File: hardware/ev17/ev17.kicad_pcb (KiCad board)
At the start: 4 copper layers, 125 x 80 mm, 185 parts, among them CN1 Conn_05x02_Female, CN2 PJ-242, J1 USB_C_Receptacle, J10 Conn_02x05_Counter_Clockwise, J11 Conn_02x05_Counter_Clockwise, J17 Conn_01x01, J18 Conn_01x01, J19 Conn_01x01, J2 Conn_01x02_Socket, J3 AudioJack4, J4 Conn_02x03_Odd_Even, J5 Conn_02x03_Odd_Even, J6 Conn_02x05_Counter_Clockwise, J7 Conn_02x05_Counter_Clockwise, J8 Conn_02x05_Counter_Clockwise, J9 Conn_02x05_Counter_Clockwise, Q1 2N7002, Q2 2N7002, Q3 2N7002, SW1 SW_SPDT, SW2 SW_Push, SW3 SW_Push, SW4 SW_Push, SW5 SW_Push, SW6 SW_Push, SW7 SW_Push, U1 BQ21040DBV, U10 STM32F405RGTx, U12 XC6227C301MR-G, U2 USBLC6-2P6, U3 STM32F072CBTx, U4 CH340C, U5 TPS63060, U6 WM8960CGEFL/RV, U7 ESP32-S3-WROOM-1, U8 M24C02-RMN6TP, U9 TPS2116DRL, Y1 Crystal_GND24

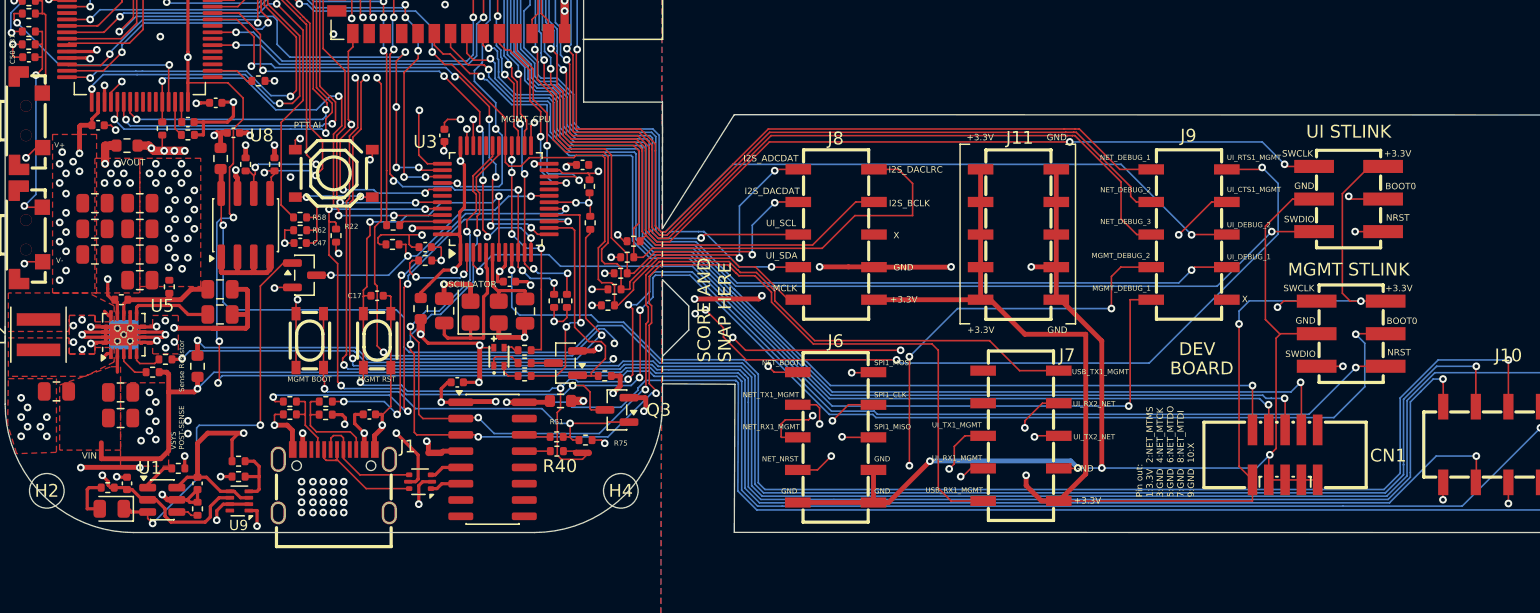
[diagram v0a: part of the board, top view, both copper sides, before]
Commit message: Moved the position of the battery charger and added a heat sink area (refs #147, #127)
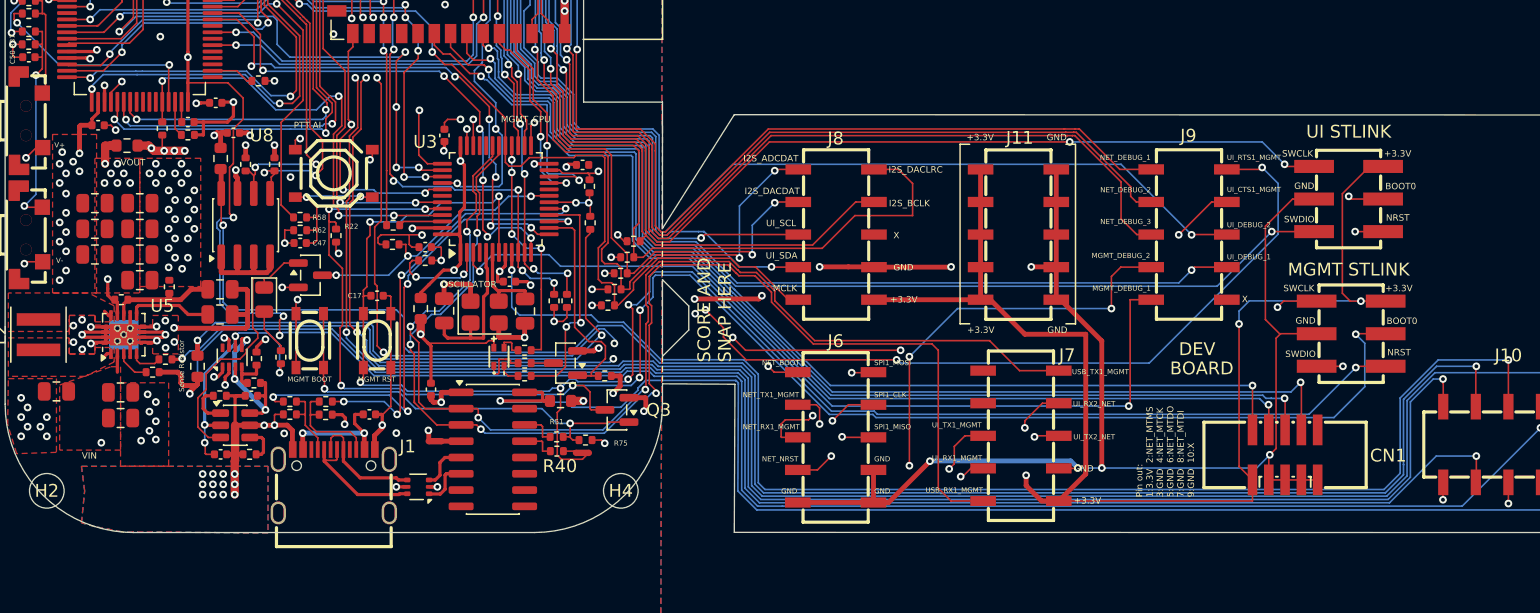
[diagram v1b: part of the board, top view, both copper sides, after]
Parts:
- moved D1 20.2 mm to (70.2, 91.8), turned to -90 degrees
- moved R11 16.9 mm to (71.5, 96.3), turned to 90 degrees
- moved U9 11.2 mm to (67.7, 96.3), turned to 90 degrees
- moved R47 9.31 mm to (69.6, 96.4), turned to -90 degrees
- moved U1 8.13 mm to (67.9, 101.6)
- moved C4 8.02 mm to (69.2, 99.3), turned to 180 degrees
- moved C12 7.64 mm to (66.8, 103.9), turned to 0 degrees
- moved R6 6.52 mm to (66.7, 99.3)
- moved R53 6.22 mm to (69.4, 98.3), turned to 0 degrees
- moved R1 5.87 mm to (69.1, 103.9), turned to 180 degrees
- moved C13 2.12 mm to (83.2, 98.8), turned to -90 degrees
- moved NT2 0.91 mm to (83.5, 102.9)
- moved U4 0.78 mm to (88.0, 103.5)
- moved Q2 0.46 mm to (73.8, 89.9)
- moved U2 0.43 mm to (82.2, 106.4)
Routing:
- net GND: track 386.4 -> 363.8 mm, vias 168 -> 155
- net Net-(J2-Pin_2): track 78.5 -> 91.5 mm, vias 2 -> 5
- net Net-(D1-K): track 31.1 -> 21.9 mm, vias 2 -> 0
- net /BB_Vin_Sense: track 131.2 -> 137.0 mm, vias 2 -> 3
- net +3.3V: track 267.4 -> 262.3 mm, vias 69 -> 65
- net Net-(SW1-C): track 76.2 -> 72.5 mm, vias 1 -> 2
- net VBUS: track 37.8 -> 34.9 mm, vias 4 -> 8
- net /UI_Sense: track 197.2 -> 194.3 mm
- net /BB_Vout_Sense: track 132.2 -> 134.8 mm
- net VSYS: track 184.8 -> 187.1 mm
- net /CH340C_Sense: track 107.7 -> 109.7 mm
- net /D_N: track 9.17 -> 11.0 mm
- net /WM8960_Sense: track 192.7 -> 191.1 mm
- net Net-(U9-PR1): track 5.01 -> 3.45 mm
- net /USB_RX1_MGMT: track 96.6 -> 95.1 mm
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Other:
- board text removed: "VSYS POST-SENSE"

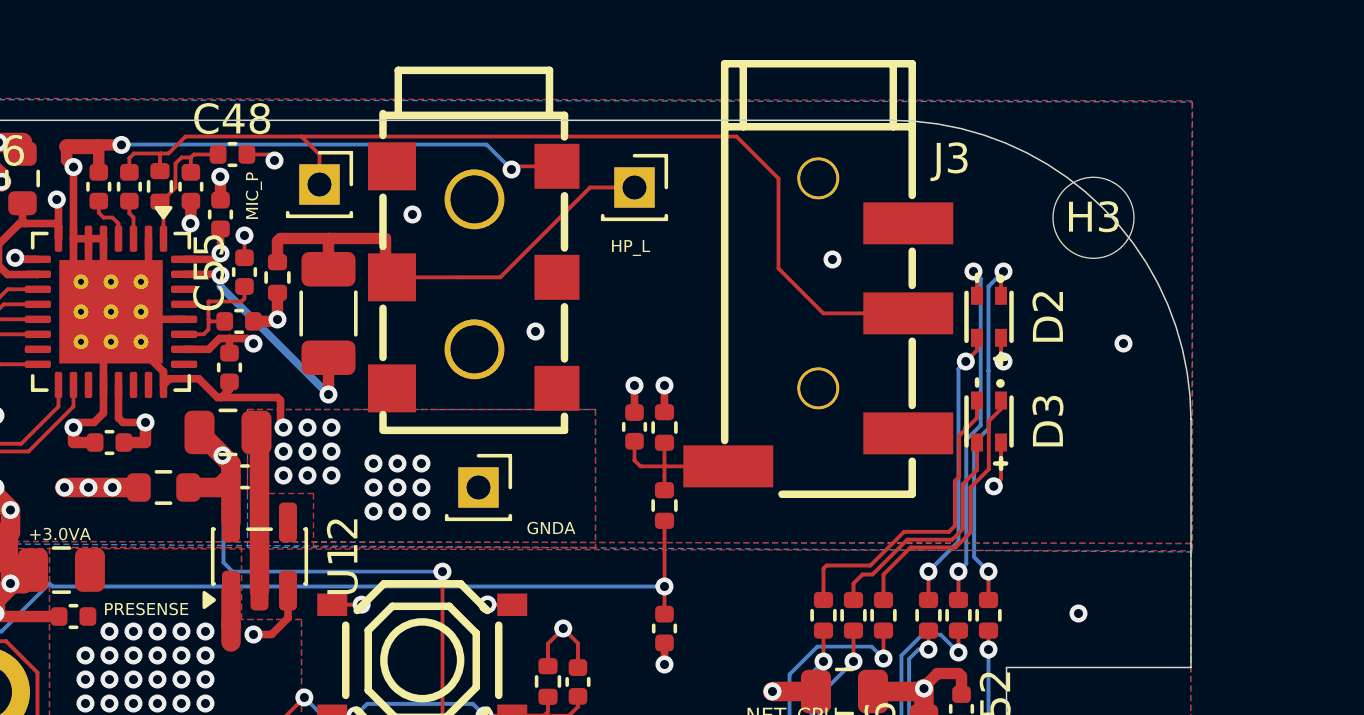
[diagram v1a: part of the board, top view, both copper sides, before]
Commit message: Added labels for the jacks (refs #410)
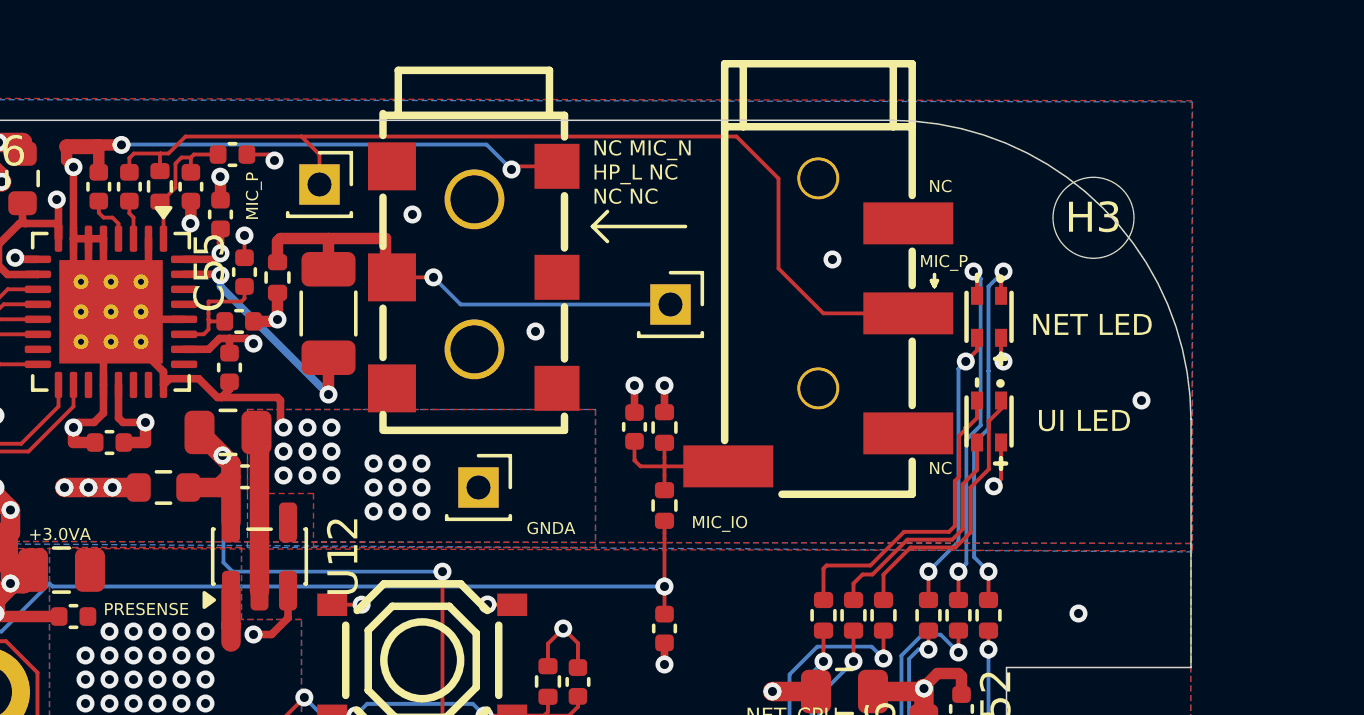
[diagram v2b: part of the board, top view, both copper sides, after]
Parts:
- moved J17 4.08 mm to (83.9, 36.1)
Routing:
- net /HP_L: track 15.9 -> 16.4 mm, vias 0 -> 1
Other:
- board text added: "MIC_IO"
- board text added: "NC"
- board text added: "NC MIC_N HP_L NC NC NC"
- board text added: "NET LED"
- board text added: "UI LED"
- board text removed: "HP_L"
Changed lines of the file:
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@@
 			(at 0 -1.16 0)
 			(layer "F.SilkS")
+			(hide yes)
 			(effects
 				(font
@@
 			(at 4.45 -6.195 0)
 			(layer "F.SilkS")
+			(hide yes)
 			(effects
 				(font
@@
 	(footprint "Connector_PinSocket_2.00mm:PinSocket_1x01_P2.00mm_Vertical"
 		(layer "F.Cu")
-		(at 82.7 32.24)
+		(at 83.9 36.14)
 		(descr "Through hole straight socket strip, 1x01, 2.00mm pitch, single row (from Kicad 4.0.7), script generated")
 		(tags "Through hole socket strip THT 1x01 2.00mm single row")
@@
 			(at 0 -2 90)
 			(layer "F.SilkS")
+			(hide yes)
 			(effects
 				(font
@@
 			(at 0 -2 90)
 			(layer "F.SilkS")
+			(hide yes)
 			(effects
 				(font
@@
 	)
 	(gr_line
+		(start 81.3 33.54)
+		(end 81.8 34.04)
+		(stroke
+			(width 0.12)
+			(type default)
+		)
+		(layer "F.SilkS")
+	)
+	(gr_line
 		(start 101.25 86.54)
 		(end 101.25 90.34)
@@
 	)
 	(gr_line
+		(start 92.7 35.54)
+		(end 92.6 35.34)
+		(stroke
+			(width 0.12)
+			(type default)
+		)
+		(layer "F.SilkS")
+	)
+	(gr_line
 		(start 125.2 79.73)
 		(end 124.45 79.73)
@@
 	)
 	(gr_line
+		(start 81.3 33.54)
+		(end 81.8 33.04)
+		(stroke
+			(width 0.12)
+			(type default)
+		)
+		(layer "F.SilkS")
+	)
+	(gr_line
 		(start 69.4 57.39)
 		(end 69.4 55.29)
@@
 	)
 	(gr_line
+		(start 92.7 35.14)
+		(end 92.7 35.54)
+		(stroke
+			(width 0.12)
+			(type default)
+		)
+		(layer "F.SilkS")
+	)
+	(gr_line
 		(start 70.2 57.04)
 		(end 70.2 55.94)
@@
 	)
 	(gr_line
+		(start 92.6 35.34)
+		(end 92.7 35.54)
+		(stroke
+			(width 0.12)
+			(type default)
+		)
+		(layer "F.SilkS")
+	)
+	(gr_line
+		(start 92.7 35.54)
+		(end 92.8 35.34)
+		(stroke
+			(width 0.12)
+			(type default)
+		)
+		(layer "F.SilkS")
+	)
+	(gr_line
+		(start 84.4 33.54)
+		(end 81.3 33.54)
+		(stroke
+			(width 0.12)
+			(type default)
+		)
+		(layer "F.SilkS")
+	)
+	(gr_line
 		(start 71 56.99)
 		(end 71 56.64)
@@
 		)
 	)
+	(gr_text "MIC_IO"
+		(at 84.6 43.64 0)
+		(layer "F.SilkS")
+		(effects
+			(font
+				(size 0.4 0.4)
+				(thickness 0.1)
+			)
+			(justify left bottom)
+		)
+	)
+	(gr_text "UI LED"
+		(at 96.1 40.44 0)
+		(layer "F.SilkS")
+		(effects
+			(font
+				(size 0.7 0.7)
+				(thickness 0.1)
+			)
+			(justify left bottom)
+		)
+	)
 	(gr_text "SWCLK"
 		(at 149.65 91.25 0)
@@
 		)
 	)
+	(gr_text "NET LED"
+		(at 95.9 37.24 0)
+		(layer "F.SilkS")
+		(effects
+			(font
+				(size 0.7 0.7)
+				(thickness 0.1)
+			)
+			(justify left bottom)
+		)
+	)
 	(gr_text "UI_RX1_MGMT"
 		(at 122.25 104.43 0)
@@
 		)
 	)
+	(gr_text "NC"
+		(at 92.5 32.44 0)
+		(layer "F.SilkS")
+		(effects
+			(font
+				(size 0.4 0.4)
+				(thickness 0.1)
+			)
+			(justify left bottom)
+		)
+	)
 	(gr_text "X"
 		(at 119.25 87.125 0)
@@
 		)
 	)
+	(gr_text "NC"
+		(at 92.5 41.84 0)
+		(layer "F.SilkS")
+		(effects
+			(font
+				(size 0.4 0.4)
+				(thickness 0.1)
+			)
+			(justify left bottom)
+		)
+	)
 	(gr_text "PRESENSE"
 		(at 65 46.54 0)
@@
 		)
 	)
-	(gr_text "HP_L"
-		(at 81.9 34.44 0)
+	(gr_text "NC MIC_N\nHP_L NC\nNC NC"
+		(at 81.3 32.84 0)
 		(layer "F.SilkS")
 		(effects
 			(font
-				(size 0.4 0.4)
+				(size 0.5 0.5)
 				(thickness 0.1)
 			)
@@
 		)
 	)
+	(gr_text "MIC_P"
+		(at 92.2 34.94 0)
+		(layer "F.SilkS")
+		(effects
+			(font
+				(size 0.4 0.4)
+				(thickness 0.1)
+			)
+			(justify left bottom)
+		)
+	)
 	(gr_text "GND"
 		(at 131.25 94.5 0)
@@
 	)
 	(segment
-		(start 82.7 32.24)
-		(end 81.219 32.24)
-		(width 0.13)
+		(start 74.616 35.235)
+		(end 76 35.235)
+		(width 0.127)
 		(layer "F.Cu")
 		(net 26)
@@
 	)
 	(segment
-		(start 76.776 35.235)
-		(end 74.816 35.235)
-		(width 0.127)
-		(layer "F.Cu")
-		(net 26)
-	)
-	(segment
 		(start 72.5 34.965)
 		(end 72.5 33.94)
@@
 	)
 	(segment
-		(start 78.224 35.235)
-		(end 81.219 32.24)
-		(width 0.13)
+		(start 74.4 35.019)
+		(end 74.616 35.235)
+		(width 0.381)
 		(layer "F.Cu")
 		(net 26)
 	)
+	(via
+		(at 76 35.235)
+		(size 0.6)
+		(drill 0.3)
+		(layers "F.Cu" "B.Cu")
+		(net 26)
+	)
 	(segment
-		(start 76.776 35.235)
-		(end 78.224 35.235)
-		(width 0.13)
-		(layer "F.Cu")
+		(start 76.905 36.14)
+		(end 83.9 36.14)
+		(width 0.127)
+		(layer "B.Cu")
 		(net 26)
 	)
 	(segment
-		(start 74.4 35.019)
-		(end 74.616 35.235)
-		(width 0.381)
-		(layer "F.Cu")
+		(start 76 35.235)
+		(end 76.905 36.14)
+		(width 0.127)
+		(layer "B.Cu")
 		(net 26)
 	)
@@
 	)
 	(via
-		(at 99 37.44)
+		(at 99.6 39.34)
 		(size 0.6)
 		(drill 0.3)

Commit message: Label cleanup
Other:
- board text added: "EEPROM"
- board text added: "MGMT"
- board text added: "NET"
- board text added: "UI"
- board text removed: "MGMT_CPU"
- board text removed: "NET_CPU"
- board text removed: "PRESENSE"
- board text removed: "UI_CPU"
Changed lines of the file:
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@@
 			(at 7 1.25 180)
 			(layer "F.SilkS")
+			(hide yes)
 			(effects
 				(font
@@
 			(at -1.26 -0.25 90)
 			(layer "F.SilkS")
+			(hide yes)
 			(effects
 				(font
@@
 			(at -1.75 0 0)
 			(layer "F.SilkS")
+			(hide yes)
 			(effects
 				(font
@@
 			(at 0 -1.43 90)
 			(layer "F.SilkS")
+			(hide yes)
 			(effects
 				(font
@@
 			(unlocked yes)
 			(layer "F.SilkS")
+			(hide yes)
 			(effects
 				(font
@@
 			(at 7.74 2.21 180)
 			(layer "F.SilkS")
+			(hide yes)
 			(effects
 				(font
@@
 			(at 5.75 -2.71 0)
 			(layer "F.SilkS")
+			(hide yes)
 			(effects
 				(font
@@
 			(at 4.46 -5.5 0)
 			(layer "F.SilkS")
+			(hide yes)
 			(effects
 				(font
@@
 			(at 2.25 3 180)
 			(layer "F.SilkS")
+			(hide yes)
 			(effects
 				(font
@@
 			(at -0.233624 -1.17 0)
 			(layer "F.SilkS")
+			(hide yes)
 			(effects
 				(font
@@
 			(at 0 2.8 270)
 			(layer "F.SilkS")
+			(hide yes)
 			(effects
 				(font
@@
 			(at -0.1 3.36 90)
 			(layer "F.SilkS")
+			(hide yes)
 			(effects
 				(font
@@
 			(at 0 -1.68 0)
 			(layer "F.SilkS")
+			(hide yes)
 			(effects
 				(font
@@
 			(at 0 -3 90)
 			(layer "F.SilkS")
+			(hide yes)
 			(effects
 				(font
@@
 			(at -3.25 0 0)
 			(layer "F.SilkS")
+			(hide yes)
 			(effects
 				(font
@@
 			(at 0 -1.43 90)
 			(layer "F.SilkS")
+			(hide yes)
 			(effects
 				(font
@@
 			(at 0 -1.16 90)
 			(layer "F.SilkS")
+			(hide yes)
 			(effects
 				(font
@@
 			(at 0 -1.16 90)
 			(layer "F.SilkS")
+			(hide yes)
 			(effects
 				(font
@@
 			(at 1.27 0 90)
 			(layer "F.SilkS")
+			(hide yes)
 			(effects
 				(font
@@
 	)
 	(gr_line
-		(start 68.6 57.04)
-		(end 68.6 55.94)
+		(start 68.2 55.49)
+		(end 68.2 54.39)
 		(stroke
 			(width 0.25)
@@
 	)
 	(gr_line
-		(start 67 57.04)
-		(end 67 55.94)
+		(start 66.6 55.49)
+		(end 66.6 54.39)
 		(stroke
 			(width 0.25)
@@
 	)
 	(gr_line
-		(start 69.4 57.39)
-		(end 69.4 55.29)
+		(start 69 55.84)
+		(end 69 53.74)
 		(stroke
 			(width 0.25)
@@
 	)
 	(gr_line
-		(start 70.2 57.04)
-		(end 70.2 55.94)
+		(start 69.8 55.49)
+		(end 69.8 54.39)
 		(stroke
 			(width 0.25)
@@
 	)
 	(gr_line
-		(start 66.2 57.39)
-		(end 66.2 55.29)
+		(start 65.8 55.84)
+		(end 65.8 53.74)
 		(stroke
 			(width 0.25)
@@
 	)
 	(gr_line
-		(start 67.8 57.04)
-		(end 67.8 56.64)
+		(start 67.4 55.49)
+		(end 67.4 55.09)
 		(stroke
 			(width 0.25)
@@
 	)
 	(gr_line
-		(start 71 56.99)
-		(end 71 56.64)
+		(start 70.6 55.44)
+		(end 70.6 55.09)
 		(stroke
 			(width 0.25)
@@
 	)
 	(gr_line
-		(start 64.7 57.04)
-		(end 64.7 56.64)
+		(start 64.3 55.49)
+		(end 64.3 55.09)
 		(stroke
 			(width 0.25)
@@
 	)
 	(gr_line
-		(start 65.4 57.04)
-		(end 65.4 55.94)
+		(start 65 55.49)
+		(end 65 54.39)
 		(stroke
 			(width 0.25)
@@
 		)
 	)
+	(gr_text "PTT AI"
+		(at 73.9 78.64 0)
+		(layer "F.SilkS")
+		(effects
+			(font
+				(size 0.7 0.7)
+				(thickness 0.1)
+			)
+			(justify left bottom)
+		)
+	)
 	(gr_text "BOOT0"
 		(at 157.7 93.8 0)
@@
 		)
 	)
-	(gr_text "MGMT_CPU"
+	(gr_text "MGMT"
 		(at 88.65 78.075 0)
 		(layer "F.SilkS")
 		(effects
 			(font
-				(size 0.5 0.5)
-				(thickness 0.0625)
+				(size 0.7 0.7)
+				(thickness 0.1)
+				(bold yes)
 			)
 			(justify left bottom)
@@
 		)
 	)
-	(gr_text "PTT AI"
-		(at 72.5 78.54 0)
-		(layer "F.SilkS")
-		(effects
-			(font
-				(size 0.5 0.5)
-				(thickness 0.0625)
-			)
-			(justify left bottom)
-		)
-	)
 	(gr_text "NET_NRST"
 		(at 109 104.5 0)
@@
 		)
 	)
-	(gr_text "PRESENSE"
-		(at 65 46.54 0)
-		(layer "F.SilkS")
-		(effects
-			(font
-				(size 0.4 0.4)
-				(thickness 0.1)
-			)
-			(justify left bottom)
-		)
-	)
 	(gr_text "CISCO"
-		(at 65.4 58.89 0)
+		(at 65 57.34 0)
 		(layer "F.SilkS")
 		(effects
@@
 	)
 	(gr_text "EV17MK1"
-		(at 64 53.04 0)
+		(at 63.6 51.49 0)
 		(layer "F.SilkS")
 		(effects
@@
 		)
 	)
+	(gr_text "EEPROM"
+		(at 70.4 80.94 90)
+		(layer "F.SilkS")
+		(effects
+			(font
+				(size 0.7 0.7)
+				(thickness 0.1)
+			)
+			(justify left bottom)
+		)
+	)
 	(gr_text "Designed in Canada"
-		(at 63.3 61.04 0)
+		(at 63.1 58.44 0)
 		(layer "F.SilkS")
 		(effects
@@
 		)
 	)
-	(gr_text "NET_CPU"
-		(at 86.4 50.14 0)
+	(gr_text "NET"
+		(at 82.1 49.84 0)
 		(layer "F.SilkS")
 		(effects
 			(font
-				(size 0.5 0.5)
-				(thickness 0.0625)
+				(size 0.7 0.7)
+				(thickness 0.1)
 			)
 			(justify left bottom)
@@
 	)
 	(gr_text "2026/03/02"
-		(at 62.842857 55.04 0)
+		(at 62.442857 53.49 0)
 		(layer "F.SilkS")
 		(effects
@@
 		)
 	)
-	(gr_text "UI_CPU"
+	(gr_text "UI"
 		(at 60.725 63.9 0)
 		(layer "F.SilkS")
 		(effects
 			(font
-				(size 0.5 0.5)
-				(thickness 0.0625)
+				(size 0.7 0.7)
+				(thickness 0.1)
 			)
 			(justify left bottom)
@@
 	)
 	(gr_text "PTT"
-		(at 75.3 51.54 0)
+		(at 74.8 51.84 0)
 		(layer "F.SilkS")
 		(effects
 			(font
-				(size 0.5 0.5)
-				(thickness 0.0625)
+				(size 0.7 0.7)
+				(thickness 0.1)
 			)
 			(justify left bottom)

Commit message: DRC cleanup
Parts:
- moved C42 0.82 mm to (56.5, 62.8)
- moved R56 0.31 mm to (90.0, 46.2)
- moved R59 0.31 mm to (91.0, 46.2)
- moved R60 0.31 mm to (89.0, 46.2)
- moved C51 0.22 mm to (89.8, 48.8)
- moved R6 0.10 mm to (66.7, 99.2)
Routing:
- net GND: track 363.8 -> 361.7 mm
- net +3.3V: track 262.3 -> 263.1 mm
- net VBUS: track 34.9 -> 34.3 mm, vias 8 -> 6
- net Net-(D3-GK): track 10.5 -> 10.0 mm
